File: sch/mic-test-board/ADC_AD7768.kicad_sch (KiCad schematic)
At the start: 26 parts, among them U6 AD7768BSTZ

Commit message: pcb: commit before large routing effort
 - schematic refactor to split preamps to each mic board
 - Mic board and main board are placed
 - no tracks laid
 - critical parts selected
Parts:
- added C208, C210: 0.1uF, Capacitor_SMD:C_0603_1608Metric, symbol Device:C_Small
- added TP2: TestPoint, TestPoint:TestPoint_Pad_D1.0mm, symbol Connector:TestPoint
- C1, C10, C11, C16, C17, C19, C2, C23, C24, C25, C3, C4, C5, C6, C7, C8, C9: footprint (none) -> Capacitor_SMD:C_0603_1608Metric
- JP2: footprint (none) -> Jumper:SolderJumper-3_P1.3mm_Open_RoundedPad1.0x1.5mm_NumberLabels
- R2, R40: footprint (none) -> Resistor_SMD:R_0603_1608Metric
- TP13, TP14, TP18, TP5, TP6: footprint (none) -> TestPoint:TestPoint_Pad_D1.0mm
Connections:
- net GND: now also C208.2, C210.2
- net V_{REF}: now also C208.1, C210.1
- net at U6.30 (~{RESET}): now also TP2.1
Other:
- note added: "Enable SPI control"
- note added: "VCM can be configured to be: - Off - AVDD1/2 - 1.65 V - 2.14 V - 2.5 V Each mic board is generating its own 1.65V (mid-supply) V_{OCM}, so we've chosen OFF."
- note added: "~{RESET} is internally pulled-up"
- company: (none) -> Josh Berry
- title: (none) -> Sound Compass POC
- moved on the sheet: C7, JP2, R2

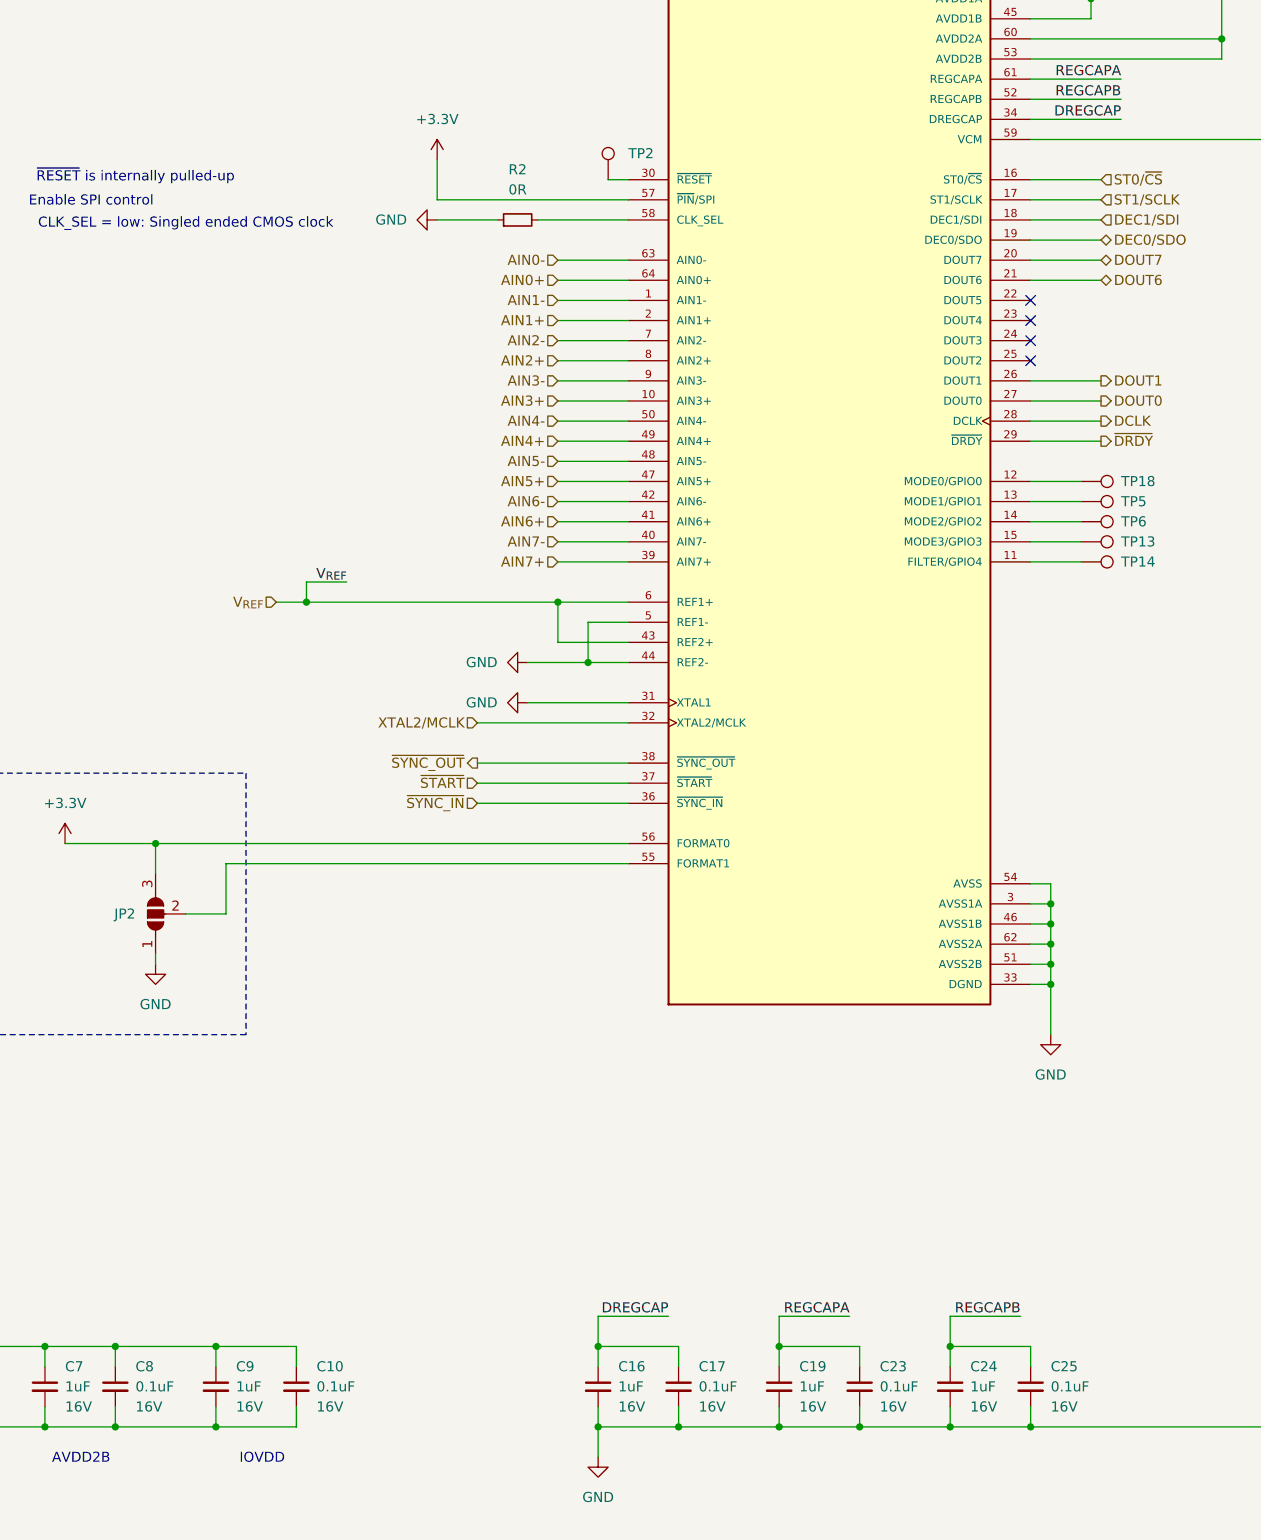
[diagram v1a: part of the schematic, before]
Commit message: pcb: finished routing mic board and ADC board.
 - BOM complete
 - uController pinout configured with CubeMX and re-checked
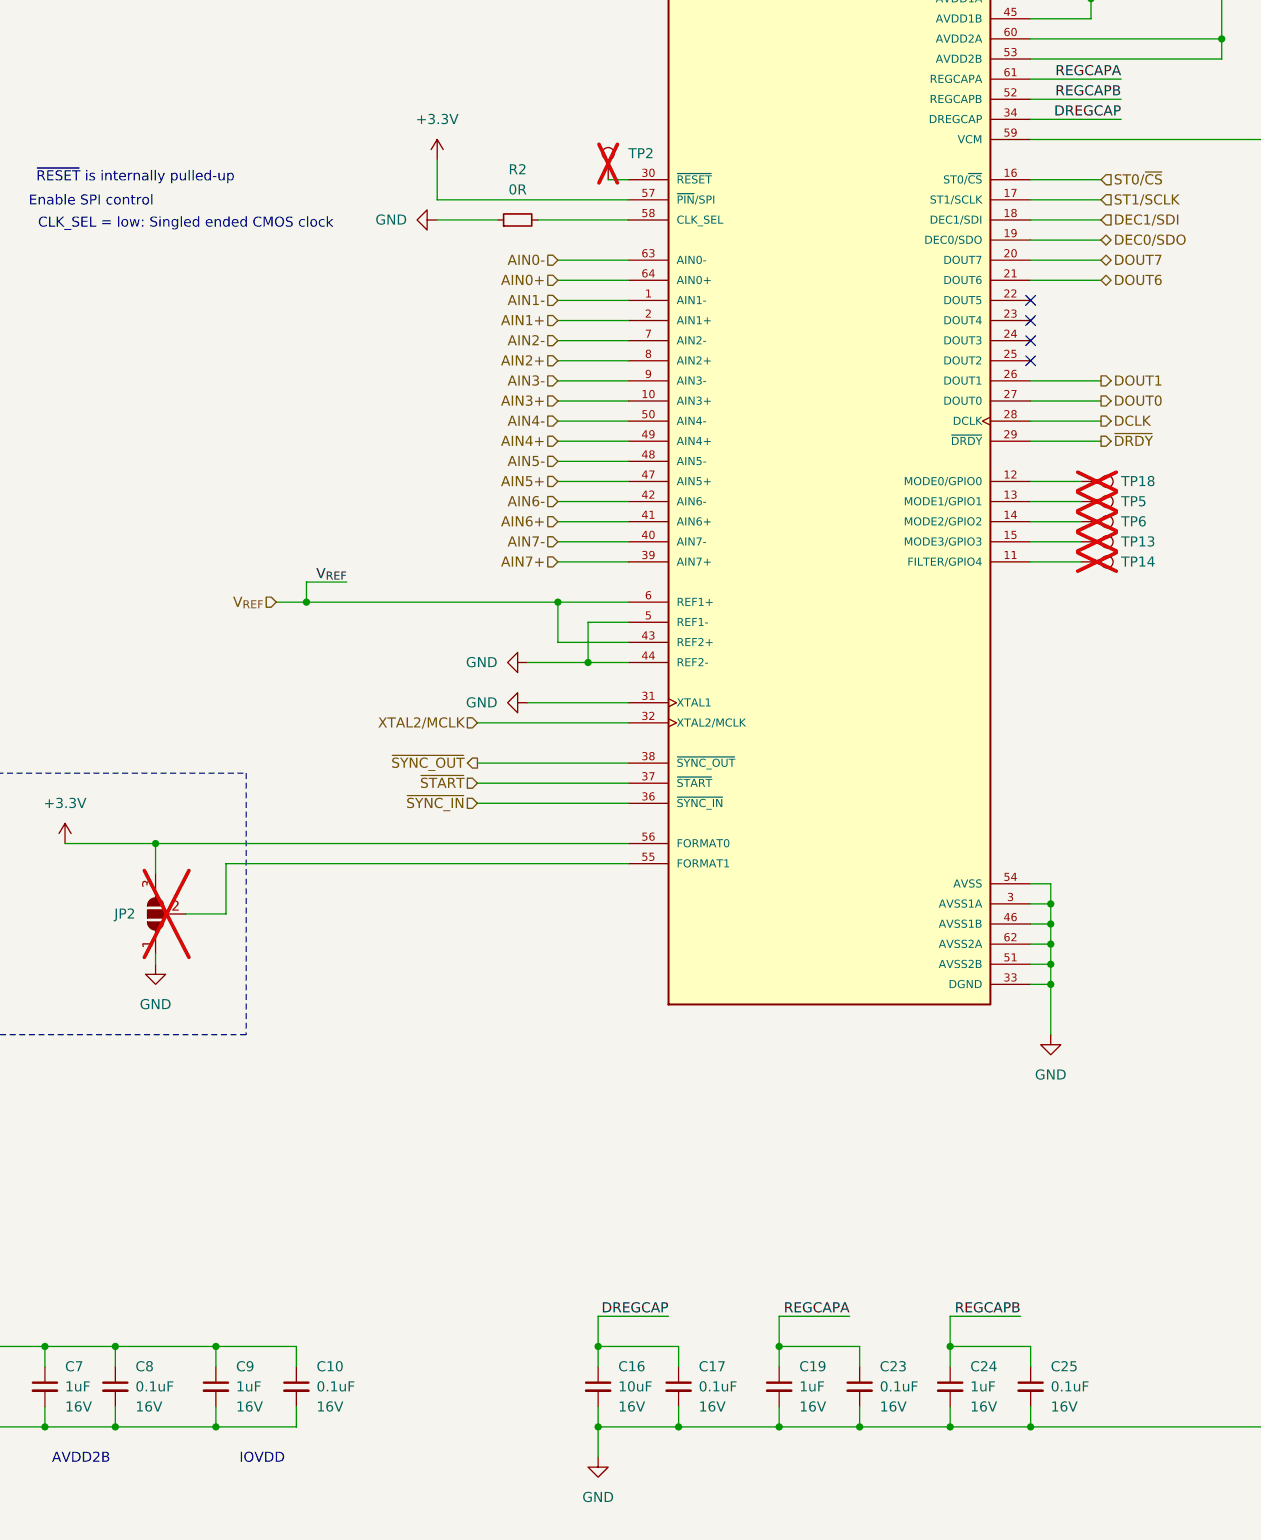
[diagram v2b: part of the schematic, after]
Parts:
- C1, C19, C24, C3, C5, C7, C9: Manufacturer (none) -> YAGEO; Part Number (none) -> CC0603KRX7R7BB105; Supplier (none) -> Digi-Key; Supplier Number (none) -> 311-1446-1-ND
- C10, C11, C17, C2, C208, C210, C23, C25, C4, C6, C8: Manufacturer (none) -> YAGEO; Part Number (none) -> CC0603KRX7R7BB104; Supplier (none) -> Digi-Key; Supplier Number (none) -> 311-1088-1-ND
- C16: value 1uF -> 10uF; footprint Capacitor_SMD:C_0603_1608Metric -> Capacitor_SMD:C_0805_2012Metric; Manufacturer (none) -> Samsung Electro-Mechanics; Part Number (none) -> CL21B106KOQNNNE; Supplier (none) -> Digi-Key; Supplier Number (none) -> 1276-2872-1-ND
- JP2, TP13, TP14, TP18, TP2, TP5, TP6: now not fitted
- R2: Manufacturer (none) -> Stackpole Electronics Inc; Part Number (none) -> RMCF0603ZT0R00; Supplier (none) -> Digi-Key; Supplier Number (none) -> RMCF0603ZT0R00CT-ND
- R40: Manufacturer (none) -> Panasonic Electronic Components; Part Number (none) -> ERJ-3EKF49R9V; Supplier (none) -> Digi-Key; Supplier Number (none) -> P49.9HCT-ND
- U6: Manufacturer (none) -> Analog Devices Inc.; Part Number (none) -> AD7768BSTZ; Supplier (none) -> Digi-Key; Supplier Number (none) -> 505-AD7768BSTZ-ND

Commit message: pcb: ordered PCB's and BOM! RevA and v240506
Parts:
- JP2, TP13, TP14, TP18, TP2, TP5, TP6: now fitted; now left out of the parts list
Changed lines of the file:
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@@
 		(unit 1)
 		(exclude_from_sim no)
-		(in_bom yes)
+		(in_bom no)
 		(on_board yes)
-		(dnp yes)
+		(dnp no)
 		(fields_autoplaced yes)
 		(property "Reference" "JP2"
@@
 		(unit 1)
 		(exclude_from_sim no)
-		(in_bom yes)
+		(in_bom no)
 		(on_board yes)
-		(dnp yes)
+		(dnp no)
 		(fields_autoplaced yes)
 		(property "Reference" "TP6"
@@
 			)
 		)
-		(property "Manufacturer" ""
+		(property "Manufacturer" "~"
 			(at 236.22 147.32 0)
 			(effects
@@
 			)
 		)
-		(property "Part Number" ""
+		(property "Part Number" "~"
 			(at 236.22 147.32 0)
 			(effects
@@
 			)
 		)
-		(property "Supplier" ""
+		(property "Supplier" "~"
 			(at 236.22 147.32 0)
 			(effects
@@
 			)
 		)
-		(property "Supplier Number" ""
+		(property "Supplier Number" "~"
 			(at 236.22 147.32 0)
 			(effects
@@
 		(unit 1)
 		(exclude_from_sim no)
-		(in_bom yes)
+		(in_bom no)
 		(on_board yes)
-		(dnp yes)
+		(dnp no)
 		(fields_autoplaced yes)
 		(property "Reference" "TP2"
@@
 			)
 		)
-		(property "Manufacturer" ""
+		(property "Manufacturer" "~"
 			(at 176.53 104.14 0)
 			(effects
@@
 			)
 		)
-		(property "Part Number" ""
+		(property "Part Number" "~"
 			(at 176.53 104.14 0)
 			(effects
@@
 			)
 		)
-		(property "Supplier" ""
+		(property "Supplier" "~"
 			(at 176.53 104.14 0)
 			(effects
@@
 			)
 		)
-		(property "Supplier Number" ""
+		(property "Supplier Number" "~"
 			(at 176.53 104.14 0)
 			(effects
@@
 		(unit 1)
 		(exclude_from_sim no)
-		(in_bom yes)
+		(in_bom no)
 		(on_board yes)
-		(dnp yes)
+		(dnp no)
 		(fields_autoplaced yes)
 		(property "Reference" "TP13"
@@
 			)
 		)
-		(property "Manufacturer" ""
+		(property "Manufacturer" "~"
 			(at 236.22 149.86 0)
 			(effects
@@
 			)
 		)
-		(property "Part Number" ""
+		(property "Part Number" "~"
 			(at 236.22 149.86 0)
 			(effects
@@
 			)
 		)
-		(property "Supplier" ""
+		(property "Supplier" "~"
 			(at 236.22 149.86 0)
 			(effects
@@
 			)
 		)
-		(property "Supplier Number" ""
+		(property "Supplier Number" "~"
 			(at 236.22 149.86 0)
 			(effects
@@
 		(unit 1)
 		(exclude_from_sim no)
-		(in_bom yes)
+		(in_bom no)
 		(on_board yes)
-		(dnp yes)
+		(dnp no)
 		(fields_autoplaced yes)
 		(property "Reference" "TP18"
@@
 			)
 		)
-		(property "Manufacturer" ""
+		(property "Manufacturer" "~"
 			(at 236.22 142.24 0)
 			(effects
@@
 			)
 		)
-		(property "Part Number" ""
+		(property "Part Number" "~"
 			(at 236.22 142.24 0)
 			(effects
@@
 			)
 		)
-		(property "Supplier" ""
+		(property "Supplier" "~"
 			(at 236.22 142.24 0)
 			(effects
@@
 			)
 		)
-		(property "Supplier Number" ""
+		(property "Supplier Number" "~"
 			(at 236.22 142.24 0)
 			(effects
@@
 		(unit 1)
 		(exclude_from_sim no)
-		(in_bom yes)
+		(in_bom no)
 		(on_board yes)
-		(dnp yes)
+		(dnp no)
 		(fields_autoplaced yes)
 		(property "Reference" "TP5"
@@
 			)
 		)
-		(property "Manufacturer" ""
+		(property "Manufacturer" "~"
 			(at 236.22 144.78 0)
 			(effects
@@
 			)
 		)
-		(property "Part Number" ""
+		(property "Part Number" "~"
 			(at 236.22 144.78 0)
 			(effects
@@
 			)
 		)
-		(property "Supplier" ""
+		(property "Supplier" "~"
 			(at 236.22 144.78 0)
 			(effects
@@
 			)
 		)
-		(property "Supplier Number" ""
+		(property "Supplier Number" "~"
 			(at 236.22 144.78 0)
 			(effects
@@
 		(unit 1)
 		(exclude_from_sim no)
-		(in_bom yes)
+		(in_bom no)
 		(on_board yes)
-		(dnp yes)
+		(dnp no)
 		(fields_autoplaced yes)
 		(property "Reference" "TP14"
@@
 			)
 		)
-		(property "Manufacturer" ""
+		(property "Manufacturer" "~"
 			(at 236.22 152.4 0)
 			(effects
@@
 			)
 		)
-		(property "Part Number" ""
+		(property "Part Number" "~"
 			(at 236.22 152.4 0)
 			(effects
@@
 			)
 		)
-		(property "Supplier" ""
+		(property "Supplier" "~"
 			(at 236.22 152.4 0)
 			(effects
@@
 			)
 		)
-		(property "Supplier Number" ""
+		(property "Supplier Number" "~"
 			(at 236.22 152.4 0)
 			(effects

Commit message: sch: adding bringup notes
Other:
- note added: "FORMATx = [FORMAT1][FORMAT0] = 01 = All channels are output in TDM mode over DOUT0, and DOUT1 Jumper config: 2-3: All channels over DOUT0 1-2: All channels split over DOUT0 + 1"
- note removed: "FORMATx = 01 = All channels are output in TDM mode over DOUT0, and DOUT1 Jumper config: 2-3: All channels over DOUT0 1-2: All channels split over DOUT0 + 1"
